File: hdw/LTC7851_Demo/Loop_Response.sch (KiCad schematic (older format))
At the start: 4 parts

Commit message: Duplicated master phase, added status LEDs and a few test points
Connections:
- wire segments 14 -> 15
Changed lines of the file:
@@
 $Descr A 11000 8500
 encoding utf-8
-Sheet 15 14
+Sheet 14 14
 Title ""
 Date ""
@@
 Wire Wire Line
 	4470 5280 4550 5280
+$Comp
+L power:GND #PWR?
+U 1 1 5BD5340B
+P 5640 4130
+F 0 "#PWR?" H 5640 3880 50  0001 C CNN
+F 1 "GND" H 5640 3980 50  0000 C CNN
+F 2 "" H 5640 4130 50  0001 C CNN
+F 3 "" H 5640 4130 50  0001 C CNN
+	1    5640 4130
+	1    0    0    -1
+$EndComp
+Wire Wire Line
+	5640 4130 5640 4050
+Connection ~ 5640 4050
 $EndSCHEMATC

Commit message: Assigned some custom footprints
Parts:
- T?: footprint (none) -> Custom Footprints Library:Murata_78601_9C; Digi-Key PN (none) -> 811-2650-ND
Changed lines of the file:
@@
 F 0 "T?" H 5000 4100 50  0000 C CNN
 F 1 "1:1 Pulse Transformer" H 5000 3550 50  0000 C CNN
-F 2 "" H 5000 3850 50  0001 C CNN
+F 2 "Custom Footprints Library:Murata_78601_9C" H 5000 3850 50  0001 C CNN
 F 3 "~" H 5000 3850 50  0001 C CNN
+F 4 "811-2650-ND" H 5000 3850 50  0001 C CNN "Digi-Key PN"
 	1    5000 3850
-	1    0    0    -1
+	-1   0    0    -1
 $EndComp
 $Comp

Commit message: Annotated schematic
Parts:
- gave numbers to parts that had none: 4
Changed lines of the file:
@@
 $EndDescr
 $Comp
-L Device:Transformer_1P_1S T?
+L Device:Transformer_1P_1S T1401
 U 1 1 5BC3161A
 P 5000 3850
-F 0 "T?" H 5000 4100 50  0000 C CNN
+F 0 "T1401" H 5000 4100 50  0000 C CNN
 F 1 "1:1 Pulse Transformer" H 5000 3550 50  0000 C CNN
 F 2 "Custom Footprints Library:Murata_78601_9C" H 5000 3850 50  0001 C CNN
@@
 $EndComp
 $Comp
-L power:+5V #PWR?
+L power:+5V #PWR01403
 U 1 1 5BC31B38
 P 4520 3570
-F 0 "#PWR?" H 4520 3420 50  0001 C CNN
+F 0 "#PWR01403" H 4520 3420 50  0001 C CNN
 F 1 "+5V" H 4520 3710 50  0000 C CNN
 F 2 "" H 4520 3570 50  0001 C CNN
@@
 LOOP_TAP
 $Comp
-L Connector_Generic:Conn_01x02 J?
+L Connector_Generic:Conn_01x02 J1403
 U 1 1 5BC3270C
 P 5960 3810
-F 0 "J?" H 5960 3910 50  0000 C CNN
+F 0 "J1403" H 5960 3910 50  0000 C CNN
 F 1 "Wave_Gen_In" H 5960 3610 50  0000 C CNN
 F 2 "" H 5960 3810 50  0001 C CNN
@@
 	5640 4050 5400 4050
 $Comp
-L Connector_Generic:Conn_01x02 J?
+L Connector_Generic:Conn_01x02 J1401
 U 1 1 5BC32CA5
 P 4750 5280
-F 0 "J?" H 4750 5380 50  0000 C CNN
+F 0 "J1401" H 4750 5380 50  0000 C CNN
 F 1 "VOUT" H 4750 5080 50  0000 C CNN
 F 2 "" H 4750 5280 50  0001 C CNN
@@
 $EndComp
 $Comp
-L Connector_Generic:Conn_01x02 J?
+L Connector_Generic:Conn_01x02 J1402
 U 1 1 5BC32CDE
 P 5660 5280
-F 0 "J?" H 5660 5380 50  0000 C CNN
+F 0 "J1402" H 5660 5380 50  0000 C CNN
 F 1 "LOOP_TAP" H 5660 5080 50  0000 C CNN
 F 2 "" H 5660 5280 50  0001 C CNN
@@
 LOOP_TAP
 $Comp
-L power:GND #PWR?
+L power:GND #PWR01404
 U 1 1 5BC32FE1
 P 5380 5460
-F 0 "#PWR?" H 5380 5210 50  0001 C CNN
+F 0 "#PWR01404" H 5380 5210 50  0001 C CNN
 F 1 "GND" H 5380 5310 50  0000 C CNN
 F 2 "" H 5380 5460 50  0001 C CNN
@@
 	5380 5380 5460 5380
 $Comp
-L power:GND #PWR?
+L power:GND #PWR01402
 U 1 1 5BC33094
 P 4470 5460
-F 0 "#PWR?" H 4470 5210 50  0001 C CNN
+F 0 "#PWR01402" H 4470 5210 50  0001 C CNN
 F 1 "GND" H 4470 5310 50  0000 C CNN
 F 2 "" H 4470 5460 50  0001 C CNN
@@
 	4470 5380 4550 5380
 $Comp
-L power:+5V #PWR?
+L power:+5V #PWR01401
 U 1 1 5BC333D8
 P 4470 5200
-F 0 "#PWR?" H 4470 5050 50  0001 C CNN
+F 0 "#PWR01401" H 4470 5050 50  0001 C CNN
 F 1 "+5V" H 4470 5340 50  0000 C CNN
 F 2 "" H 4470 5200 50  0001 C CNN
@@
 	4470 5280 4550 5280
 $Comp
-L power:GND #PWR?
+L power:GND #PWR01405
 U 1 1 5BD5340B
 P 5640 4130
-F 0 "#PWR?" H 5640 3880 50  0001 C CNN
+F 0 "#PWR01405" H 5640 3880 50  0001 C CNN
 F 1 "GND" H 5640 3980 50  0000 C CNN
 F 2 "" H 5640 4130 50  0001 C CNN

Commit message: Assigned footprints
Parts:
- J1401, J1402, J1403: footprint (none) -> Pin_Headers:Pin_Header_Straight_1x02_Pitch2.54mm
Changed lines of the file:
@@
 F 0 "J1403" H 5960 3910 50  0000 C CNN
 F 1 "Wave_Gen_In" H 5960 3610 50  0000 C CNN
-F 2 "" H 5960 3810 50  0001 C CNN
+F 2 "Pin_Headers:Pin_Header_Straight_1x02_Pitch2.54mm" H 5960 3810 50  0001 C CNN
 F 3 "~" H 5960 3810 50  0001 C CNN
 	1    5960 3810
@@
 F 0 "J1401" H 4750 5380 50  0000 C CNN
 F 1 "VOUT" H 4750 5080 50  0000 C CNN
-F 2 "" H 4750 5280 50  0001 C CNN
+F 2 "Pin_Headers:Pin_Header_Straight_1x02_Pitch2.54mm" H 4750 5280 50  0001 C CNN
 F 3 "~" H 4750 5280 50  0001 C CNN
 	1    4750 5280
@@
 F 0 "J1402" H 5660 5380 50  0000 C CNN
 F 1 "LOOP_TAP" H 5660 5080 50  0000 C CNN
-F 2 "" H 5660 5280 50  0001 C CNN
+F 2 "Pin_Headers:Pin_Header_Straight_1x02_Pitch2.54mm" H 5660 5280 50  0001 C CNN
 F 3 "~" H 5660 5280 50  0001 C CNN
 	1    5660 5280

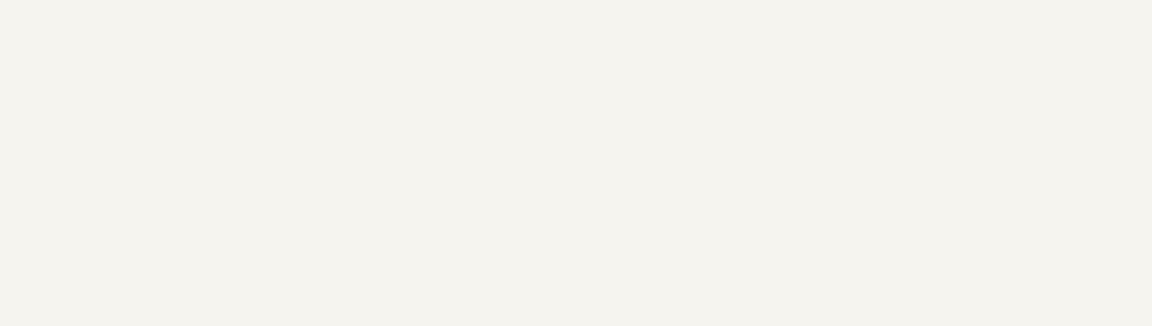
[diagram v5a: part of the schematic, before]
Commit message: Added page titles
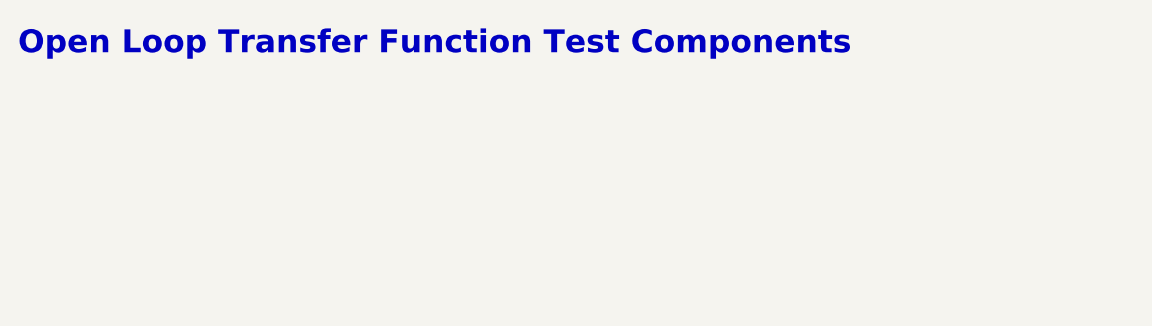
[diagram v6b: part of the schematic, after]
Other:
- note added: "Open Loop Transfer Function Test Components"
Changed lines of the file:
@@
 	5640 4130 5640 4050
 Connection ~ 5640 4050
+Text Notes 540  690  0    100  ~ 20
+Open Loop Transfer Function Test Components
 $EndSCHEMATC

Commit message: Substantial wiring and layout changes
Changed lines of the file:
@@
 L Connector_Generic:Conn_01x02 J1401
 U 1 1 5BC32CA5
-P 4750 5280
-F 0 "J1401" H 4750 5380 50  0000 C CNN
-F 1 "VOUT" H 4750 5080 50  0000 C CNN
-F 2 "Pin_Headers:Pin_Header_Straight_1x02_Pitch2.54mm" H 4750 5280 50  0001 C CNN
-F 3 "~" H 4750 5280 50  0001 C CNN
-	1    4750 5280
+P 4600 5280
+F 0 "J1401" H 4600 5380 50  0000 C CNN
+F 1 "VOUT" H 4600 5080 50  0000 C CNN
+F 2 "Pin_Headers:Pin_Header_Straight_1x02_Pitch2.54mm" H 4600 5280 50  0001 C CNN
+F 3 "~" H 4600 5280 50  0001 C CNN
+	1    4600 5280
 	1    0    0    -1
 $EndComp
@@
 L power:GND #PWR01402
 U 1 1 5BC33094
-P 4470 5460
-F 0 "#PWR01402" H 4470 5210 50  0001 C CNN
-F 1 "GND" H 4470 5310 50  0000 C CNN
-F 2 "" H 4470 5460 50  0001 C CNN
-F 3 "" H 4470 5460 50  0001 C CNN
-	1    4470 5460
+P 4320 5460
+F 0 "#PWR01402" H 4320 5210 50  0001 C CNN
+F 1 "GND" H 4320 5310 50  0000 C CNN
+F 2 "" H 4320 5460 50  0001 C CNN
+F 3 "" H 4320 5460 50  0001 C CNN
+	1    4320 5460
 	1    0    0    -1
 $EndComp
 Wire Wire Line
-	4470 5460 4470 5380
+	4320 5460 4320 5380
 Wire Wire Line
-	4470 5380 4550 5380
+	4320 5380 4400 5380
 $Comp
 L power:+5V #PWR01401
 U 1 1 5BC333D8
-P 4470 5200
-F 0 "#PWR01401" H 4470 5050 50  0001 C CNN
-F 1 "+5V" H 4470 5340 50  0000 C CNN
-F 2 "" H 4470 5200 50  0001 C CNN
-F 3 "" H 4470 5200 50  0001 C CNN
-	1    4470 5200
+P 4320 5200
+F 0 "#PWR01401" H 4320 5050 50  0001 C CNN
+F 1 "+5V" H 4320 5340 50  0000 C CNN
+F 2 "" H 4320 5200 50  0001 C CNN
+F 3 "" H 4320 5200 50  0001 C CNN
+	1    4320 5200
 	1    0    0    -1
 $EndComp
 Wire Wire Line
-	4470 5200 4470 5280
+	4320 5200 4320 5280
 Wire Wire Line
-	4470 5280 4550 5280
+	4320 5280 4400 5280
 $Comp
 L power:GND #PWR01405
